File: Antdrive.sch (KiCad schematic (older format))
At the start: 28 parts, among them J1 Conn_01x06, J2 Conn_01x03, J3 Conn_01x03, M1 Conn_01x02, M2 Conn_01x02, Q1 MMBT3904, U1 AMS1117-5.0, U2 STM32F030F4Px, U3 DRV8848, U5 HT75xx-1-SOT89

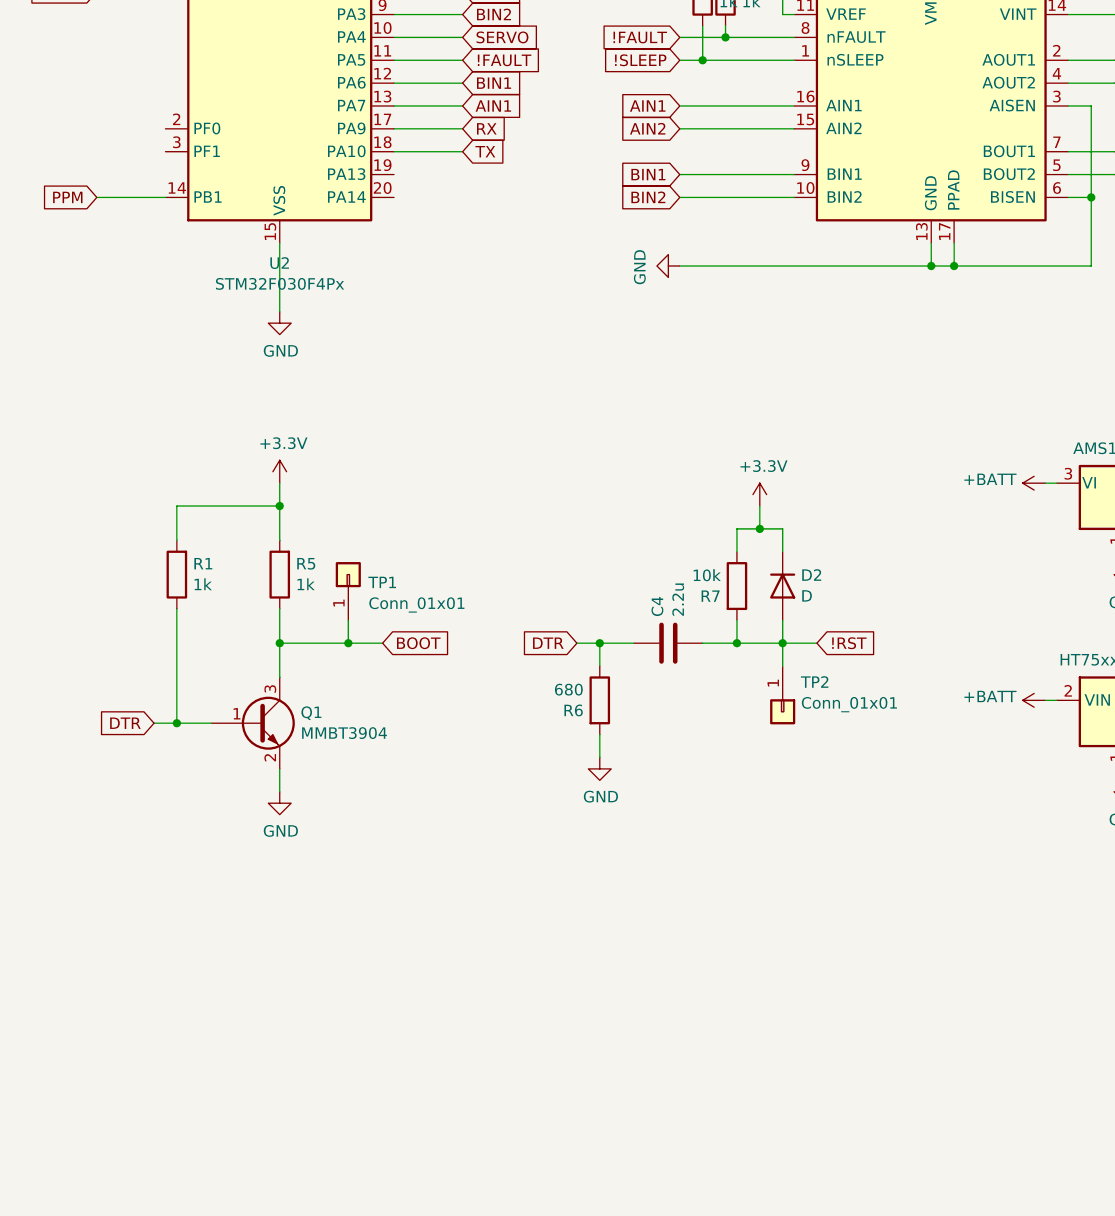
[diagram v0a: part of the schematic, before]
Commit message: Ver 0.3
Added config jumpers and hopefully fixed programming circuitry
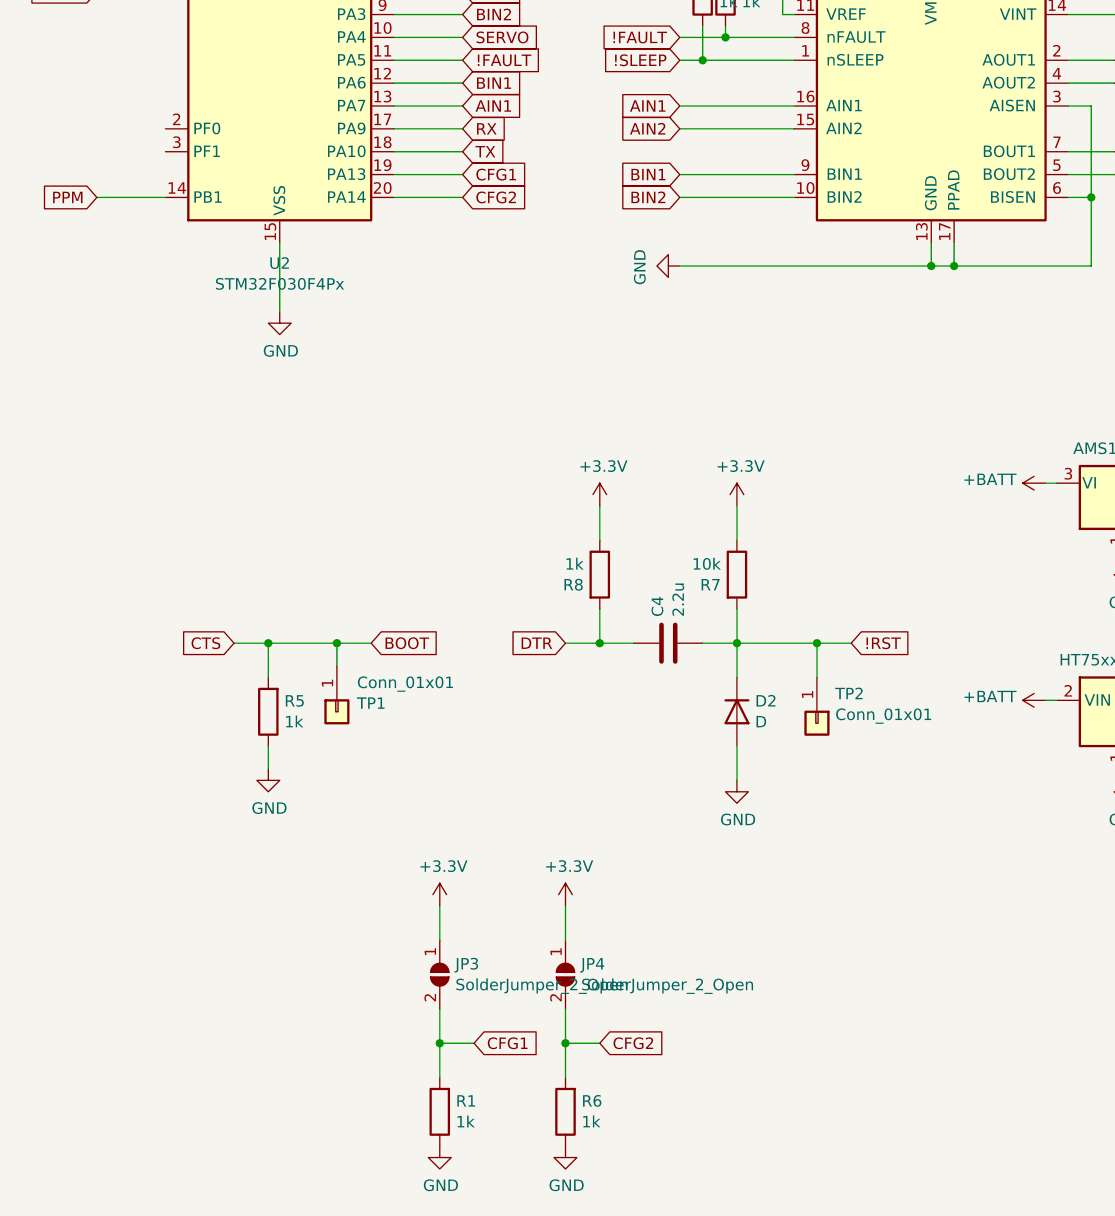
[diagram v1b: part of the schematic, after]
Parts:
- removed Q1: MMBT3904, Package_TO_SOT_SMD:SOT-23, symbol Transistor_BJT:MMBT3904
- added JP3, JP4: SolderJumper_2_Open, Jumper:SolderJumper-2_P1.3mm_Open_Pad1.0x1.5mm, symbol Jumper:SolderJumper_2_Open
- added R8: 1k, Resistor_SMD:R_0603_1608Metric, symbol Device:R
- R6: value 680 -> 1k
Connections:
- net CTS is gone; now on net BOOT: J1.2 (Pin_2)
- net !RST: now also D2.1 (K); no longer D2.2 (A)
- net +3V3: now also JP3.1 (A), JP4.1 (A), R8.1; no longer D2.1 (K), R1.2, R5.2
- net BOOT: now also R5.2; no longer R5.1
- net DTR: now also R8.2; no longer R1.1, R6.1
- net GND: now also D2.2 (A), R1.1, R5.1, R6.1; no longer R6.2
- net CFG1: now reaches U2.19 (PA13)
- net CFG1: now also R1.2, JP3.2 (B)
- net CFG2: now reaches U2.20 (PA14)
- net CFG2: now also R6.2, JP4.2 (B)
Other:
- moved on the sheet: D2, R5, R7, TP1, TP2

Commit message: Added documentation
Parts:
- R5: value 1k -> 100k
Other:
- note added: "1.0"
- note added: "14/07/2020"
- note added: "Antdrive"
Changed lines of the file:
@@
 	5850 1300 5850 1750
-$Comp
-L Device:R R2
-U 1 1 5EA341EC
-P 4000 1650
-F 0 "R2" H 3930 1604 50  0000 R CNN
-F 1 "1k" H 3930 1695 50  0000 R CNN
-F 2 "Resistor_SMD:R_0603_1608Metric" V 3930 1650 50  0001 C CNN
-F 3 "~" H 4000 1650 50  0001 C CNN
-	1    4000 1650
-	-1   0    0    1
-$EndComp
 $Comp
 L Device:R R3
@@
 P 2100 4800
 F 0 "R5" H 2030 4754 50  0000 R CNN
-F 1 "1k" H 2030 4845 50  0000 R CNN
+F 1 "100k" H 2030 4845 50  0000 R CNN
 F 2 "Resistor_SMD:R_0603_1608Metric" V 2030 4800 50  0001 C CNN
 F 3 "~" H 2100 4800 50  0001 C CNN
@@
 Text GLabel 3550 6250 2    50   Input ~ 0
 CFG2
+Text Notes 8125 7640 0    50   ~ 0
+14/07/2020
+Text Notes 7345 7520 0    100  ~ 0
+Antdrive
+Text Notes 10575 7645 0    50   ~ 0
+1.0
+$Comp
+L Device:R R2
+U 1 1 5EA341EC
+P 4000 1650
+F 0 "R2" H 3930 1604 50  0000 R CNN
+F 1 "1k" H 3930 1695 50  0000 R CNN
+F 2 "Resistor_SMD:R_0603_1608Metric" V 3930 1650 50  0001 C CNN
+F 3 "~" H 4000 1650 50  0001 C CNN
+	1    4000 1650
+	1    0    0    1
+$EndComp
 $EndSCHEMATC
